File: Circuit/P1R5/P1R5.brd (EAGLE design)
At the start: 61 x 61 mm, 126 parts, among them U1 MK20DX256VLH7, Y1 32.768KHz, Y2 16Mhz/8pF

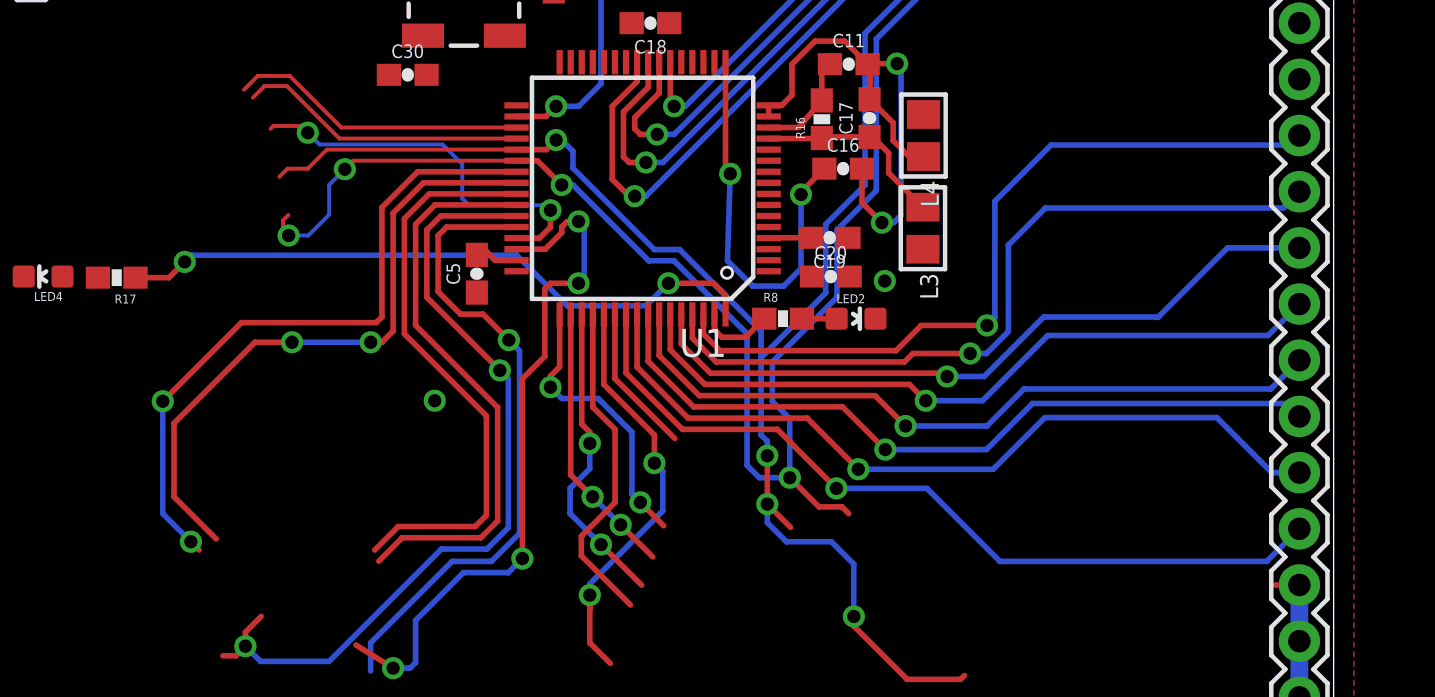
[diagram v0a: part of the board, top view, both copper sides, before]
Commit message: more cleanup on micro.
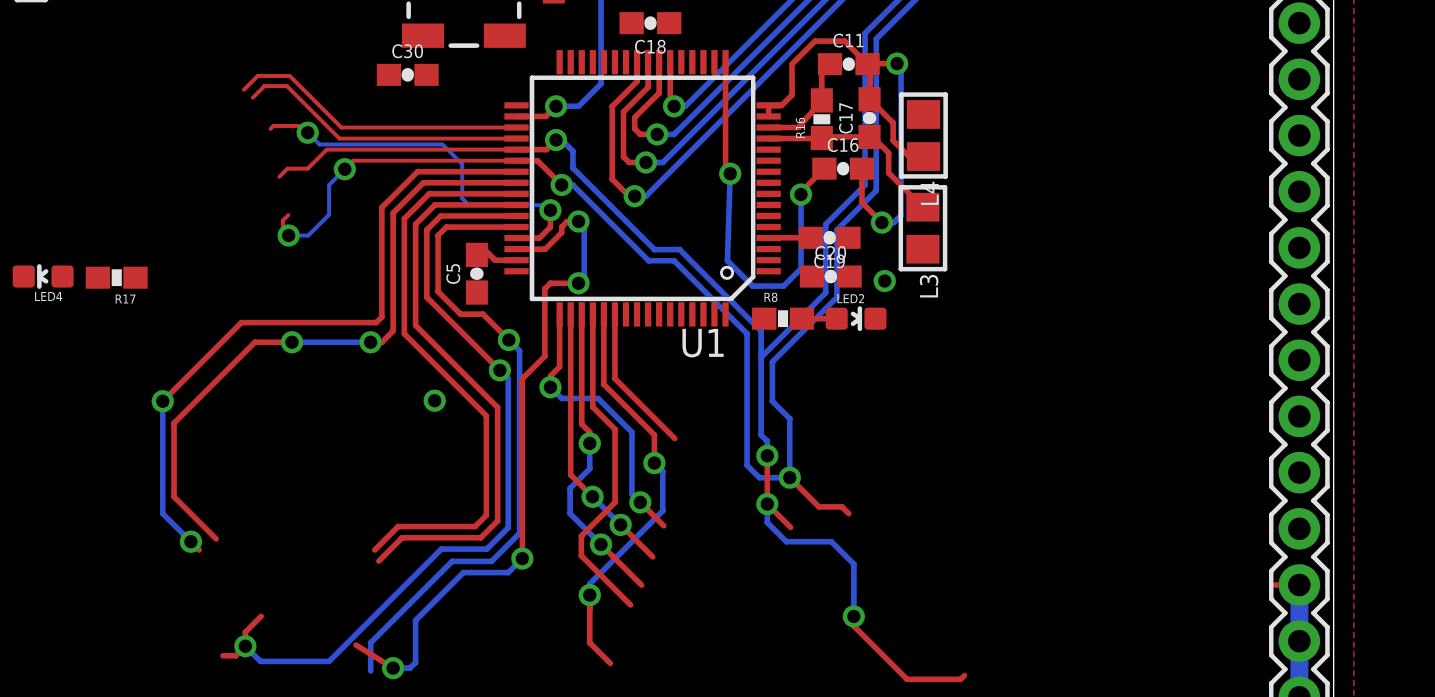
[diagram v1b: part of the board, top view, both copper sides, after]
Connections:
- net PTC10 renamed N$24
- net PTC11 renamed N$16
- net PTD0 renamed N$17
- net PTD1 renamed N$18
- net PTD2 renamed N$19
- net PTD3 renamed N$20
- net PTD4 renamed N$21
- net PTD5 renamed N$23
- removed net PTD6: R8.1, U1.63
- removed net PTD7: R17.1, U1.64
- new net N$10: LED2.C, U1.63
- new net N$13: LED4.C, U1.64
- net 3.3V: now also R17.1, R8.1
- net GND: no longer LED2.C, LED4.C
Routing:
- net N$24: track 37.2 -> 0.00 mm, vias 1 -> 0
- net N$16: track 36.2 -> 0.00 mm, vias 1 -> 0
- net N$23: track 35.3 -> 0.00 mm, vias 1 -> 0
- net N$21: track 34.4 -> 0.00 mm, vias 1 -> 0
- net N$17: track 34.3 -> 0.00 mm, vias 1 -> 0
- net N$18: track 33.4 -> 0.00 mm, vias 1 -> 0
- net N$19: track 32.8 -> 0.00 mm, vias 1 -> 0
- net N$20: track 32.3 -> 0.00 mm, vias 1 -> 0
- net PTD7: track 29.5 -> 0.00 mm, vias 2 -> 0
- net PTD6: track 3.43 -> 0.00 mm

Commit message: hierarchical blocks done.
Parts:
- removed IMU1:R13, IMU1:R14: 10k, SparkFun-Resistors:0603-RES
- added R13, R14: 10k, SparkFun-Resistors:0603-RES
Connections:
- net PTB0 renamed N$27
- net PTB1 renamed N$28
- net PTB16 renamed N$34
- net PTB17 renamed N$35
- net PTB18 renamed N$38
- net PTB19 renamed N$39
- net PTC1 renamed N$41
- net PTC3 renamed N$40
- net PTC4 renamed N$46
- net PTC5 renamed N$47
- net PTC6 renamed N$48
- net PTC7 renamed N$49
- net PTC8 renamed N$42
- net PTC9 renamed N$45
- removed net A12: U1.11
- removed net A13: U1.12
- removed net AD0: U1.45
- removed net DAC/A14: U1.18
- removed net IMU1:GND: IMU1:C24.1, IMU1:C25.2, IMU1:C27.1, IMU1:U3.18, IMU1:U3.20
- removed net LED_DRIVER1:GND: LED_DRIVER1:R19.2, LED_DRIVER1:R20.2, LED_DRIVER1:R21.2, LED_DRIVER1:R23.2, LED_DRIVER1:R24.2, LED_DRIVER1:U$20.9, LED_DRIVER1:U$21.9
- removed net MESH1:GND: MESH1:C10.2, MESH1:C12.2, MESH1:C14.2, MESH1:C15.2, MESH1:C36.2, MESH1:C37.1, MESH1:C8.1, MESH1:C9.2, MESH1:R12.2, MESH1:U$4.14, MESH1:U$4.17, MESH1:U$4.20, MESH1:U$4.8
- removed net PTA12: U1.28
- removed net PTA13: U1.29
- removed net PTA4: U1.26
- removed net PTA5: U1.27
- removed net PTC0: U1.43
- removed net PTE0: U1.1
- removed net PTE1: U1.2
- removed net SCL: U1.37
- removed net SDA: U1.38
- removed net USB_D_N: U1.6
- removed net USB_D_P: U1.5
- removed net WIFI1:GND: WIFI1:C22.1, WIFI1:C23.2, WIFI1:C26.1, WIFI1:C28.1, WIFI1:C33.2, WIFI1:C34.2, WIFI1:C35.2, WIFI1:C7.2, WIFI1:L7.2, WIFI1:L8.2, WIFI1:R1.2, WIFI1:R5.1, WIFI1:R51.1, WIFI1:U$3.4, WIFI1:U$6.GND
- new net N$25: R14.2, U1.37
- new net N$26: R13.2, U1.38
- net 3.3V: now also R13.1, R14.1
- net GND: now also IMU1:C24.1, IMU1:C25.2, IMU1:C27.1, IMU1:U3.18, IMU1:U3.20, LED_DRIVER1:R19.2, LED_DRIVER1:R20.2, LED_DRIVER1:R21.2, LED_DRIVER1:R23.2, LED_DRIVER1:R24.2, LED_DRIVER1:U$20.9, LED_DRIVER1:U$21.9, MESH1:C10.2, MESH1:C12.2, MESH1:C14.2, MESH1:C15.2, MESH1:C36.2, MESH1:C37.1, MESH1:C8.1, MESH1:C9.2, MESH1:R12.2, MESH1:U$4.14, MESH1:U$4.17, MESH1:U$4.20, MESH1:U$4.8, WIFI1:C22.1, WIFI1:C23.2, WIFI1:C26.1, WIFI1:C28.1, WIFI1:C33.2, WIFI1:C34.2, WIFI1:C35.2, WIFI1:C7.2, WIFI1:L7.2, WIFI1:L8.2, WIFI1:R1.2, WIFI1:R5.1, WIFI1:R51.1, WIFI1:U$3.4, WIFI1:U$6.GND
- net IMU1:N$1: no longer IMU1:R13.2
- net IMU1:N$2: no longer IMU1:R14.2
- net IMU1:N$6: no longer IMU1:R13.1, IMU1:R14.1
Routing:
- net SCL: track 87.3 -> 0.00 mm, vias 5 -> 0
- net SDA: track 78.5 -> 0.00 mm, vias 5 -> 0
- net PTC0: track 36.8 -> 0.00 mm, vias 2 -> 0
- net N$40: track 31.7 -> 0.00 mm, vias 4 -> 0
- net N$34: track 30.6 -> 0.00 mm, vias 2 -> 0
- net N$41: track 29.3 -> 0.00 mm, vias 1 -> 0
- net N$35: track 29.1 -> 0.00 mm, vias 2 -> 0
- net N$38: track 26.2 -> 0.00 mm
- net N$39: track 26.0 -> 0.00 mm
- net N$42: track 19.3 -> 0.00 mm, vias 2 -> 0
- net AD0: track 18.1 -> 0.00 mm, vias 2 -> 0
- net N$49: track 15.1 -> 0.00 mm
- net N$48: track 14.1 -> 0.00 mm, vias 2 -> 0
- net N$27: track 13.5 -> 0.00 mm
- net N$28: track 13.1 -> 0.00 mm
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
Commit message: labels made on all hierarchical blocks and nets
pretty much all connected back up. Not sure it's showing through on the
schematic yet.
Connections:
- new net N$50: U1.43
- new net WIFI1:N$25: WIFI1:C33.2, WIFI1:U$6.VDDA/1
- new net WIFI1:N$26: WIFI1:C26.2, WIFI1:U$6.VDD3P3/3
- new net WIFI1:N$27: WIFI1:C28.2, WIFI1:U$6.VDD3P3/4
- net 3.3V: now also WIFI1:R15.2
- net GND: now also WIFI1:C33.1; no longer WIFI1:C33.2
- net WIFI1:N$17: no longer WIFI1:C26.2, WIFI1:C28.2, WIFI1:C33.1, WIFI1:R15.2, WIFI1:U$6.VDD3P3/3, WIFI1:U$6.VDD3P3/4, WIFI1:U$6.VDDA/1
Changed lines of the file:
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@@
 <contactref element="WIFI1:C34" pad="2"/>
 <contactref element="WIFI1:L7" pad="2"/>
-<contactref element="WIFI1:C33" pad="2"/>
 <contactref element="WIFI1:C7" pad="2"/>
-<contactref element="WIFI1:C28" pad="1"/>
-<contactref element="WIFI1:C26" pad="1"/>
 <contactref element="WIFI1:C23" pad="2"/>
 <contactref element="WIFI1:R1" pad="2"/>
@@
 <contactref element="LED_DRIVER1:U$20" pad="9"/>
 <contactref element="LED_DRIVER1:U$21" pad="9"/>
+<contactref element="WIFI1:C33" pad="1"/>
+<contactref element="WIFI1:C26" pad="1"/>
+<contactref element="WIFI1:C28" pad="1"/>
 <wire x1="-22.8482" y1="-200.6854" x2="-22.8482" y2="-203.6572" width="0" layer="19" extent="1-1"/>
 <wire x1="-22.8482" y1="-194.7418" x2="-22.8482" y2="-200.6854" width="0" layer="19" extent="1-1"/>
@@
 <wire x1="-5.8302" y1="-55.88" x2="-7.5302" y2="-61.8236" width="0" layer="19" extent="1-1"/>
 <wire x1="-5.8302" y1="-52.9082" x2="-5.8302" y2="-55.88" width="0" layer="19" extent="1-1"/>
-<wire x1="-5.8302" y1="-49.9364" x2="-5.8302" y2="-52.9082" width="0" layer="19" extent="1-1"/>
-<wire x1="-7.5302" y1="-46.9646" x2="-5.8302" y2="-49.9364" width="0" layer="19" extent="1-1"/>
+<wire x1="-7.5302" y1="-49.9364" x2="-5.8302" y2="-52.9082" width="0" layer="19" extent="1-1"/>
+<wire x1="-7.5302" y1="-46.9646" x2="-7.5302" y2="-49.9364" width="0" layer="19" extent="1-1"/>
 <wire x1="-7.5302" y1="-43.9928" x2="-7.5302" y2="-46.9646" width="0" layer="19" extent="1-1"/>
 <wire x1="-5.588" y1="-40.0812" x2="-7.5302" y2="-43.9928" width="0" layer="19" extent="1-1"/>
@@
 <contactref element="R14" pad="1"/>
 <contactref element="R13" pad="1"/>
+<contactref element="WIFI1:R15" pad="2"/>
 <wire x1="45.466" y1="55.2958" x2="48.6814" y2="54.0258" width="0" layer="19" extent="1-1"/>
 <wire x1="36.307" y1="54.356" x2="45.466" y2="55.2958" width="0" layer="19" extent="1-1"/>
@@
 <wire x1="6.7936" y1="31.496" x2="24.018" y2="31.7846" width="0" layer="19" extent="1-1"/>
 <wire x1="58.3268" y1="17.6022" x2="42.3926" y2="32.7812" width="0" layer="19" extent="1-1"/>
-<wire x1="-7.5302" y1="-64.7954" x2="6.7936" y2="31.496" width="0" layer="19" extent="1-1"/>
+<wire x1="-5.8302" y1="-58.8518" x2="6.7936" y2="31.496" width="0" layer="19" extent="1-1"/>
+<wire x1="-7.5302" y1="-64.7954" x2="-5.8302" y2="-58.8518" width="0" layer="19" extent="1-1"/>
 <wire x1="-7.1492" y1="-68.0212" x2="-7.5302" y2="-64.7954" width="0" layer="19" extent="1-1"/>
 <wire x1="-11.0664" y1="-69.4454" x2="-7.1492" y2="-68.0212" width="0" layer="19" extent="1-1"/>
@@
 <contactref element="WIFI1:C22" pad="2"/>
 <contactref element="WIFI1:C34" pad="1"/>
-<contactref element="WIFI1:C33" pad="1"/>
-<contactref element="WIFI1:C28" pad="2"/>
-<contactref element="WIFI1:C26" pad="2"/>
 <contactref element="WIFI1:U$3" pad="8"/>
-<contactref element="WIFI1:R15" pad="2"/>
 <contactref element="WIFI1:C35" pad="1"/>
-<contactref element="WIFI1:U$6" pad="VDDA/1"/>
-<contactref element="WIFI1:U$6" pad="VDD3P3/3"/>
-<contactref element="WIFI1:U$6" pad="VDD3P3/4"/>
 <contactref element="WIFI1:U$6" pad="VDDPST/11"/>
 <contactref element="WIFI1:U$6" pad="VDDPST/17"/>
 <contactref element="WIFI1:U$6" pad="VDDD/29"/>
 <contactref element="WIFI1:U$6" pad="VDDA/30"/>
-<wire x1="-7.5302" y1="-55.88" x2="-5.8302" y2="-58.8518" width="0" layer="19" extent="1-1"/>
 <wire x1="-7.5302" y1="-52.9082" x2="-7.5302" y2="-55.88" width="0" layer="19" extent="1-1"/>
-<wire x1="-7.5302" y1="-49.9364" x2="-7.5302" y2="-52.9082" width="0" layer="19" extent="1-1"/>
-<wire x1="-5.8302" y1="-46.9646" x2="-7.5302" y2="-49.9364" width="0" layer="19" extent="1-1"/>
-<wire x1="-5.8302" y1="-43.9928" x2="-5.8302" y2="-46.9646" width="0" layer="19" extent="1-1"/>
-<wire x1="-6.338" y1="-42.3812" x2="-5.8302" y2="-43.9928" width="0" layer="19" extent="1-1"/>
-<wire x1="-7.888" y1="-39.8312" x2="-6.338" y2="-42.3812" width="0" layer="19" extent="1-1"/>
-<wire x1="-7.888" y1="-39.3312" x2="-7.888" y2="-39.8312" width="0" layer="19" extent="1-1"/>
-<wire x1="-7.888" y1="-38.3312" x2="-7.888" y2="-39.3312" width="0" layer="19" extent="1-1"/>
-<wire x1="-6.338" y1="-37.7812" x2="-7.888" y2="-38.3312" width="0" layer="19" extent="1-1"/>
+<wire x1="-6.338" y1="-42.3812" x2="-7.5302" y2="-52.9082" width="0" layer="19" extent="1-1"/>
+<wire x1="-3.288" y1="-41.8312" x2="-6.338" y2="-42.3812" width="0" layer="19" extent="1-1"/>
+<wire x1="-6.338" y1="-37.7812" x2="-6.338" y2="-42.3812" width="0" layer="19" extent="1-1"/>
 <wire x1="-5.838" y1="-37.7812" x2="-6.338" y2="-37.7812" width="0" layer="19" extent="1-1"/>
-<wire x1="-3.288" y1="-41.8312" x2="-6.338" y2="-42.3812" width="0" layer="19" extent="1-1"/>
 <wire x1="-5.8302" y1="-28.1686" x2="-5.838" y2="-37.7812" width="0" layer="19" extent="1-1"/>
 <wire x1="-3.388" y1="-22.9396" x2="-5.8302" y2="-28.1686" width="0" layer="19" extent="1-1"/>
@@
 </signal>
 <signal name="WIFI1:N$11">
-<contactref element="WIFI1:C7" pad="1"/>
 <contactref element="WIFI1:Y3" pad="1"/>
 <contactref element="WIFI1:U$6" pad="XTAL_OUT/27"/>
+<contactref element="WIFI1:C7" pad="1"/>
 <wire x1="-7.0062" y1="-20.7334" x2="-4.838" y2="-37.7812" width="0" layer="19" extent="1-1"/>
 <wire x1="-7.5302" y1="-15.4686" x2="-7.0062" y2="-20.7334" width="0" layer="19" extent="1-1"/>
@@
 <signal name="WIFI1:N$12">
 <contactref element="WIFI1:Y3" pad="3"/>
+<contactref element="WIFI1:U$6" pad="XTAL_IN/28"/>
 <contactref element="WIFI1:C23" pad="1"/>
-<contactref element="WIFI1:U$6" pad="XTAL_IN/28"/>
 <wire x1="-3.3062" y1="-18.4334" x2="-5.338" y2="-37.7812" width="0" layer="19" extent="1-1"/>
 <wire x1="-7.5302" y1="-12.4968" x2="-3.3062" y2="-18.4334" width="0" layer="19" extent="1-1"/>
@@
 <contactref element="U1" pad="52"/>
 </signal>
+<signal name="N$50">
+<contactref element="U1" pad="43"/>
+</signal>
+<signal name="WIFI1:N$25">
+<contactref element="WIFI1:C33" pad="2"/>
+<contactref element="WIFI1:U$6" pad="VDDA/1"/>
+<wire x1="-7.888" y1="-38.3312" x2="-5.8302" y2="-49.9364" width="0" layer="19" extent="1-1"/>
+</signal>
+<signal name="WIFI1:N$26">
+<contactref element="WIFI1:C26" pad="2"/>
+<contactref element="WIFI1:U$6" pad="VDD3P3/3"/>
+<wire x1="-7.888" y1="-39.3312" x2="-5.8302" y2="-43.9928" width="0" layer="19" extent="1-1"/>
+</signal>
+<signal name="WIFI1:N$27">
+<contactref element="WIFI1:C28" pad="2"/>
+<contactref element="WIFI1:U$6" pad="VDD3P3/4"/>
+<wire x1="-7.888" y1="-39.8312" x2="-5.8302" y2="-46.9646" width="0" layer="19" extent="1-1"/>
+</signal>
 </signals>

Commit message: moved libraries, regenerated PCB, reannotated design, connected hierarchical blocks.
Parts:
- removed C16, C18, C19, C21, VREG1:C2, VREG1:C4: 0.1uF, appfruits:0603-CAP
- removed C17, C20: 2.2uF, appfruits:0603-CAP
- removed C29, C30, C31, C32, VREG1:C1: 10uF, appfruits:0603-CAP
- removed IMU1:C24, IMU1:C25, IMU1:C27, MESH1:C36, MESH1:C37, WIFI1:C26, WIFI1:C28, WIFI1:C33, WIFI1:C34, WIFI1:C35: .1 uF, SparkFun-Capacitors:0603-CAP
- removed IMU1:U3: MPU-9250, chips:QFN-24/3MM
- removed JP5: (no value), SparkFun-Connectors:1X02
- removed L3, L4: 600 Ohm/100 Mhz, appfruits:0805
- removed LED4, VREG1:LED1: (no value), appfruits:LED-0603
- removed LED_DRIVER1:JP3: (no value), SparkFun:1X04
- removed LED_DRIVER1:R19, LED_DRIVER1:R20, LED_DRIVER1:R21, LED_DRIVER1:R22, LED_DRIVER1:R23, LED_DRIVER1:R24: 10k, SparkFun:0603-RES
- removed LED_DRIVER1:R25, LED_DRIVER1:R26, LED_DRIVER1:R27, LED_DRIVER1:R28, LED_DRIVER1:R29, LED_DRIVER1:R30, LED_DRIVER1:R31, LED_DRIVER1:R32, LED_DRIVER1:R33, LED_DRIVER1:R34, LED_DRIVER1:R35, LED_DRIVER1:R36, LED_DRIVER1:R37, LED_DRIVER1:R38, LED_DRIVER1:R39, LED_DRIVER1:R40, LED_DRIVER1:R41, LED_DRIVER1:R42, LED_DRIVER1:R43, LED_DRIVER1:R44, LED_DRIVER1:R45, LED_DRIVER1:R46, LED_DRIVER1:R47, LED_DRIVER1:R48, R49, R50, R52, R53: (no value), SparkFun:0402-RES
- removed LED_DRIVER1:U$11, LED_DRIVER1:U$13, LED_DRIVER1:U$14, LED_DRIVER1:U$15, LED_DRIVER1:U$16, LED_DRIVER1:U$17, LED_DRIVER1:U$18, LED_DRIVER1:U$8: LTST-C19FD1WT, led:LTST-C19FD1WT
- removed LED_DRIVER1:U$20, LED_DRIVER1:U$21: PCA9552BS, NXP_By_element14_Batch_1:HVQFN24
- removed MESH1:C10: 4.7 pF, SparkFun-Capacitors:0603-CAP
- removed MESH1:C12: 1.0 pF, SparkFun-Capacitors:0603-CAP
- removed MESH1:C13: 1.5 pF, SparkFun-Capacitors:0603-CAP
- removed MESH1:C14, MESH1:C15: 22 pF, SparkFun-Capacitors:0603-CAP
- removed MESH1:C8: 33 nF, SparkFun-Capacitors:0603-CAP
- removed MESH1:C9: 2.2 nF, SparkFun-Capacitors:0603-CAP
- removed MESH1:L2: 2.7 nH, SparkFun-Passives:C0402
- removed MESH1:L5: 8.2 nH, SparkFun-Passives:C0402
- removed MESH1:L6: 3.9 nH, SparkFun-Passives:C0402
- removed MESH1:R11: 1M, SparkFun-Resistors:0603-RES
- removed MESH1:R12: 22k, SparkFun-Resistors:0603-RES
- removed MESH1:U$2, WIFI1:U$1: ANTENNA2SMD, SparkFun-RF:ANTENNA-CHIP2
- removed MESH1:U$4: NRF24L01, RF:QFN20(4X4)
- removed MESH1:Y4: 16 Mhz, SparkFun-FreqCtrl:CRYSTAL-SMD-5X3
- removed R13, R14, WIFI1:R51: 10k, SparkFun-Resistors:0603-RES
- removed R16, R17, VREG1:R9: 470, appfruits:0603-RES
- removed U$7: 2X5_0.05"_CORTEX_DEBUGTH_NOKEY_UNSHROUDED, con-cortex:2X5_0.05"_TH_NS
- removed VREG1:C3: 22uF, appfruits:0603-CAP
- removed VREG1:L1: 2.2uH, 2.1A, appfruits:LPS3015
- removed VREG1:R3: 2M, appfruits:0603-RES
- removed VREG1:R4, VREG1:R6: 220K, appfruits:0603-RES
- removed VREG1:R7: 1.2M, appfruits:0603-RES
- removed VREG1:U2: TPS61200, appfruits:QFN-10_PAD
- removed WIFI1:C22: 1 uF, SparkFun-Capacitors:0603-CAP
- removed WIFI1:C23, WIFI1:C7: 15 pF, SparkFun-Capacitors:0603-CAP
- removed WIFI1:C6: 5.6 pF, SparkFun-Capacitors:0603-CAP
- removed WIFI1:L7, WIFI1:L8: (no value), SparkFun-Passives:0603
- removed WIFI1:R1, WIFI1:R15, WIFI1:R5: 12k, SparkFun-Resistors:0603-RES
- removed WIFI1:R18: 200, SparkFun-Resistors:0603-RES
- removed WIFI1:U$3: 25Q40, wifi:SOP8
- removed WIFI1:U$6: ESP8266EX, wifi:QFN32
- removed WIFI1:Y3: 26 Mhz, SparkFun-FreqCtrl:CRYSTAL-SMD-5X3
- added C1, C7: 2.2uF, appfruits:0603-CAP
- added C10, C101, C12, C9: 10uF, appfruits:0603-CAP
- added C102, C104, C2, C3, C4, C6, C8: 0.1uF, appfruits:0603-CAP
- added C103: 22uF, appfruits:0603-CAP
- added C206: 5.6 pF, SparkFun-Capacitors:0603-CAP
- added C207, C223: 15 pF, SparkFun-Capacitors:0603-CAP
- added C222: 1 uF, SparkFun-Capacitors:0603-CAP
- added C226, C228, C233, C234, C235, C336, C337, C424, C425, C427: .1 uF, SparkFun-Capacitors:0603-CAP
- added C308: 33 nF, SparkFun-Capacitors:0603-CAP
- added C309: 2.2 nF, SparkFun-Capacitors:0603-CAP
- added C310: 4.7 pF, SparkFun-Capacitors:0603-CAP
- added C312: 1.0 pF, SparkFun-Capacitors:0603-CAP
- added C313: 1.5 pF, SparkFun-Capacitors:0603-CAP
- added C314, C315: 22 pF, SparkFun-Capacitors:0603-CAP
- added J1: 2X5_0.05"_CORTEX_DEBUGTH_NOKEY_UNSHROUDED, con-cortex:2X5_0.05"_TH_NS
- added JP2: (no value), SparkFun-Connectors:1X15
- added JP503: (no value), SparkFun:1X04
- added L1, L2: 600 Ohm/100 Mhz, appfruits:0805
- added L101: 2.2uH, 2.1A, appfruits:LPS3015
- added L207, L208: DNP, SparkFun-Passives:0603
- added L302: 2.7 nH, SparkFun-Passives:C0402
- added L305: 8.2 nH, SparkFun-Passives:C0402
- added L306: 3.9 nH, SparkFun-Passives:C0402
- added LED1, LED101: (no value), appfruits:LED-0603
- added R1, R109, R6, R7: 470, appfruits:0603-RES
- added R103: 2M, appfruits:0603-RES
- added R104, R106: 220K, appfruits:0603-RES
- added R107: 1.2M, appfruits:0603-RES
- added R2, R3, R4, R5, R525, R526, R527, R528, R529, R530, R531, R532, R533, R534, R535, R536, R537, R538, R539, R540, R541, R542, R543, R544, R545, R546, R547, R548: (no value), SparkFun:0402-RES
- added R201, R205, R215: 12k, SparkFun-Resistors:0603-RES
- added R218: 200, SparkFun-Resistors:0603-RES
- added R251, R9: 10k, SparkFun-Resistors:0603-RES
- added R311: 1M, SparkFun-Resistors:0603-RES
- added R312: 22k, SparkFun-Resistors:0603-RES
- added R519, R520, R521, R522, R523, R524: 10k, SparkFun:0603-RES
- added U$201, U$302: ANTENNA2SMD, SparkFun-RF:ANTENNA-CHIP2
- added U$203: 25Q40, wifi:SOP8
- added U$206: ESP8266EX, wifi:QFN32
- added U$304: NRF24L01, RF:QFN20(4X4)
- added U$508, U$511, U$513, U$514, U$515, U$516, U$517, U$518: LTST-C19FD1WT, led:LTST-C19FD1WT
- added U$520, U$521: PCA9552BS, NXP_By_element14_Batch_1:HVQFN24
- added U102: TPS61200, appfruits:QFN-10_PAD
- added U403: MPU-9250, chips:QFN-24/3MM
- added Y203: 26 Mhz, SparkFun-FreqCtrl:CRYSTAL-SMD-5X3
- added Y304: 16 Mhz, SparkFun-FreqCtrl:CRYSTAL-SMD-5X3
- C11: value 0.1uF -> 10uF
- JP1: device SparkFun-Connectors:1X15 -> SparkFun-Connectors:1X02
- R8: value 470 -> 10k; device appfruits:0603-RES -> SparkFun-Resistors:0603-RES
- Y1: value 32.768KHz -> 16Mhz/8pF; device appfruits:CRYSTAL-TXC-7A -> appfruits:CRYSTAL-SMD-5X3
- Y2: value 16Mhz/8pF -> 32.768KHz; device appfruits:CRYSTAL-SMD-5X3 -> appfruits:CRYSTAL-TXC-7A
- moved JP1 118.8 mm to (-57.1, 71.1), turned to 0 degrees
- moved C11 95.7 mm to (-49.5, 77.5)
- moved R8 91.4 mm to (-39.4, 81.3)
- moved LED2 81.8 mm to (-24.1, 81.3), turned to 0 degrees
- moved S1 70.7 mm to (-68.6, 66.0), turned to 0 degrees
- moved C5 67.0 mm to (-26.7, 77.5), turned to 0 degrees
- moved Y1 66.1 mm to (-31.8, 66.0), turned to 0 degrees
- moved U1 61.2 mm to (-25.4, 8.89), turned to 0 degrees
- moved Y2 53.6 mm to (-16.5, 81.3)
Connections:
- removed net IMU1:N$1: IMU1:U3.24
- removed net IMU1:N$2: IMU1:U3.23
- removed net IMU1:N$3: IMU1:U3.11
- removed net IMU1:N$5: IMU1:U3.12
- removed net IMU1:N$6: IMU1:C24.2, IMU1:C25.1, IMU1:U3.1, IMU1:U3.13, IMU1:U3.22, IMU1:U3.8
- removed net IMU1:N$7: IMU1:U3.9
- removed net LED_DRIVER1:N$31: LED_DRIVER1:U$20.20, LED_DRIVER1:U$21.20
- removed net LED_DRIVER1:N$32: LED_DRIVER1:U$20.19, LED_DRIVER1:U$21.19
- removed net LED_DRIVER1:N$34: LED_DRIVER1:U$20.21, LED_DRIVER1:U$21.21
- removed net LED_DRIVER1:N$35: LED_DRIVER1:U$21.16
- removed net LED_DRIVER1:N$36: LED_DRIVER1:U$21.17
- removed net LED_DRIVER1:V+: LED_DRIVER1:R22.2, LED_DRIVER1:U$11.V, LED_DRIVER1:U$13.V, LED_DRIVER1:U$14.V, LED_DRIVER1:U$15.V, LED_DRIVER1:U$16.V, LED_DRIVER1:U$17.V, LED_DRIVER1:U$18.V, LED_DRIVER1:U$8.V
- removed net MESH1:N$15: MESH1:C36.1, MESH1:C37.2, MESH1:U$4.15, MESH1:U$4.18, MESH1:U$4.7
- removed net MESH1:N$2: MESH1:U$4.2
- removed net MESH1:N$3: MESH1:U$4.3
- removed net MESH1:N$4: MESH1:U$4.4
- removed net MESH1:N$5: MESH1:U$4.5
- removed net MESH1:N$6: MESH1:U$4.6
- removed net MESH1:N$9: MESH1:L2.2
- removed net N$11: C18.1, C21.1, C5.1
- removed net N$19: JP1.8, U1.59
- removed net N$25: R14.2, U1.37
- removed net N$26: R13.2, U1.38
- removed net N$27: U1.35
- removed net N$28: U1.36
- removed net N$32: S1.2, VREG1:C1.1, VREG1:C2.1, VREG1:L1.2, VREG1:R3.2, VREG1:U2.5, VREG1:U2.6, VREG1:U2.8
- removed net N$34: U1.39
- removed net N$35: U1.40
- removed net N$38: U1.41
- removed net N$39: U1.42
- removed net N$40: U1.46
- removed net N$41: U1.44
- removed net N$42: U1.53
- removed net N$45: U1.54
- removed net N$46: U1.49
- removed net N$47: U1.50
- removed net N$48: U1.51
- removed net N$49: U1.52
- removed net N$50: U1.43
- removed net WIFI1:N$1: WIFI1:U$3.1, WIFI1:U$6.SD_CMD/20
- removed net WIFI1:N$10: WIFI1:U$6.U0TXD/26
- removed net WIFI1:N$13: WIFI1:R1.1, WIFI1:U$6.RES12K/31
- removed net WIFI1:N$15: WIFI1:U$6.GPIO2/14
- removed net WIFI1:N$17: WIFI1:C22.2, WIFI1:C34.1, WIFI1:C35.1, WIFI1:U$3.8, WIFI1:U$6.VDDA/30, WIFI1:U$6.VDDD/29, WIFI1:U$6.VDDPST/11, WIFI1:U$6.VDDPST/17
- removed net WIFI1:N$18: WIFI1:U$6.CHIP_EN/7
- removed net WIFI1:N$19: WIFI1:R15.1, WIFI1:U$6.EXT_RSTB/32
- removed net WIFI1:N$2: WIFI1:U$3.2, WIFI1:U$6.SD_DATA_0/22
- removed net WIFI1:N$20: WIFI1:U$6.GPIO0/15
- removed net WIFI1:N$21: WIFI1:R18.1, WIFI1:U$3.6
- removed net WIFI1:N$23: WIFI1:U$6.U0RXD/25
- removed net WIFI1:N$24: WIFI1:U$6.XPD_DCDC/8
- removed net WIFI1:N$3: WIFI1:U$3.3, WIFI1:U$6.SD_DATA_3/19
- removed net WIFI1:N$4: WIFI1:U$3.7, WIFI1:U$6.SD_DATA_2/18
- removed net WIFI1:N$6: WIFI1:U$3.5, WIFI1:U$6.SD_DATA_1/23
- removed net WIFI1:N$9: WIFI1:U$6.TOUT/6
- new net CE: U$304.1, U1.54
- new net CHANGE: JP2.8, U1.59
- new net CHIP_EN: U$206.CHIP_EN/7, U1.44
- new net CSN: U$304.2, U1.49
- new net FSYNC: U1.36, U403.11
- new net GPIO0: U$206.GPIO0/15, U1.41
- new net GPIO2: U$206.GPIO2/14, U1.42
- new net INT: U1.35, U403.12
- new net IRQ: U$304.6, U1.53
- new net MISO: U$304.5, U1.52
- new net MOSI: U$304.4, U1.51
- new net N$3: U1.45, U403.22
- new net N$4: R8.2, U$520.19, U$521.19, U1.37, U403.23
- new net SCK: U$304.3, U1.50
- new net SDA: R9.2, U$520.20, U$521.20, U1.38, U403.24
- new net U0RX: U$206.U0RXD/25, U1.40
- new net U0TX: U$206.U0TXD/26, U1.39
- new net V_IN: C101.1, C102.1, L101.2, R103.2, S1.2, U102.5, U102.6, U102.8
- new net WIFI1:CLK: R218.1, U$203.6
- new net WIFI1:CS: U$203.1, U$206.SD_CMD/20
- new net WIFI1:D0: U$203.2, U$206.SD_DATA_0/22
- new net WIFI1:DIO: U$203.5, U$206.SD_DATA_1/23
- new net WIFI1:HOLD#: U$203.7, U$206.SD_DATA_2/18
- new net WIFI1:WP#: U$203.3, U$206.SD_DATA_3/19
- new net WIFI_RESET: R215.1, U$206.EXT_RSTB/32, U1.43
- new net XPD_DCDC: U$206.XPD_DCDC/8, U1.46
- net 3.3V: now also C103.1, C2.1, C222.2, C234.1, C235.1, C3.1, C336.1, C337.2, C4.1, C424.2, C425.1, C5.1, C7.1, J1.1, JP2.13, JP2.14, JP2.15, L1.2, R107.2, R109.1, R2.1, R215.2, R4.1, R5.1, R522.2, R6.1, R7.1, R9.1, U$203.8, U$206.VDDA/30, U$206.VDDD/29, U$206.VDDPST/11, U$206.VDDPST/17, U$304.15, U$304.18, U$304.7, U$508.V, U$511.V, U$513.V, U$514.V, U$515.V, U$516.V, U$517.V, U$518.V, U$520.21, U$521.21, U102.2, U403.1, U403.13, U403.8; no longer C19.1, C20.1, JP1.13, JP1.14, JP1.15, L3.2, R13.1, R14.1, R17.1, R49.1, R52.1, R53.1, U$7.1, VREG1:C3.1, VREG1:R7.2, VREG1:R9.1, VREG1:U2.2, WIFI1:R15.2
- net GND: now also C10.1, C101.2, C103.2, C104.2, C11.1, C12.1, C2.2, C207.2, C222.1, C223.2, C226.1, C228.1, C233.1, C234.2, C235.2, C3.2, C308.1, C309.2, C310.2, C312.2, C314.2, C315.2, C336.2, C337.1, C4.2, C424.1, C425.2, C427.1, C7.2, C9.1, J1.3, J1.5, J1.9, JP2.1, JP2.2, JP2.3, JP2.4, L2.1, L207.2, L208.2, LED101.C, R104.1, R106.1, R201.2, R205.1, R251.1, R3.1, R312.2, R519.2, R520.2, R521.2, R523.2, R524.2, U$203.4, U$206.GND, U$304.14, U$304.17, U$304.20, U$304.8, U$520.9, U$521.9, U102.11, U102.12, U102.13, U102.14, U102.15, U102.4, U102.9, U403.18, U403.20, U403.9; no longer C18.2, C19.2, C20.2, C21.2, C29.1, C30.1, C31.1, C32.1, IMU1:C24.1, IMU1:C25.2, IMU1:C27.1, IMU1:U3.18, IMU1:U3.20, JP1.1, JP1.3, JP1.4, L4.1, LED_DRIVER1:R19.2, LED_DRIVER1:R20.2, LED_DRIVER1:R21.2, LED_DRIVER1:R23.2, LED_DRIVER1:R24.2, LED_DRIVER1:U$20.9, LED_DRIVER1:U$21.9, MESH1:C10.2, MESH1:C12.2, MESH1:C14.2, MESH1:C15.2, MESH1:C36.2, MESH1:C37.1, MESH1:C8.1, MESH1:C9.2, MESH1:R12.2, MESH1:U$4.14, MESH1:U$4.17, MESH1:U$4.20, MESH1:U$4.8, R50.1, U$7.3, U$7.5, U$7.9, VREG1:C1.2, VREG1:C3.2, VREG1:C4.2, VREG1:LED1.C, VREG1:R4.1, VREG1:R6.1, VREG1:U2.11, VREG1:U2.12, VREG1:U2.13, VREG1:U2.14, VREG1:U2.15, VREG1:U2.4, VREG1:U2.9, WIFI1:C22.1, WIFI1:C23.2, WIFI1:C26.1, WIFI1:C28.1, WIFI1:C33.1, WIFI1:C34.2, WIFI1:C35.2, WIFI1:C7.2, WIFI1:L7.2, WIFI1:L8.2, WIFI1:R1.2, WIFI1:R5.1, WIFI1:R51.1, WIFI1:U$3.4, WIFI1:U$6.GND
- net IMU1:N$4: now also C427.2, U403.10; no longer IMU1:C27.2, IMU1:U3.10
- net LED_DRIVER1:N$1: now also R527.1, U$520.3; no longer LED_DRIVER1:R27.1, LED_DRIVER1:U$20.3
- net LED_DRIVER1:N$10: now also R535.1, U$520.11; no longer LED_DRIVER1:R35.1, LED_DRIVER1:U$20.11
- net LED_DRIVER1:N$11: now also R536.1, U$520.12; no longer LED_DRIVER1:R36.1, LED_DRIVER1:U$20.12
- net LED_DRIVER1:N$12: now also R534.1, U$520.13; no longer LED_DRIVER1:R34.1, LED_DRIVER1:U$20.13
- net LED_DRIVER1:N$13: now also JP503.4, U$520.14; no longer LED_DRIVER1:JP3.4, LED_DRIVER1:U$20.14
- net LED_DRIVER1:N$14: now also R520.1, U$520.23; no longer LED_DRIVER1:R20.1, LED_DRIVER1:U$20.23
- net LED_DRIVER1:N$15: now also R521.1, U$520.22; no longer LED_DRIVER1:R21.1, LED_DRIVER1:U$20.22
- net LED_DRIVER1:N$16: now also R538.1, U$521.1; no longer LED_DRIVER1:R38.1, LED_DRIVER1:U$21.1
- net LED_DRIVER1:N$17: now also R539.1, U$521.2; no longer LED_DRIVER1:R39.1, LED_DRIVER1:U$21.2
- net LED_DRIVER1:N$18: now also R537.1, U$521.3; no longer LED_DRIVER1:R37.1, LED_DRIVER1:U$21.3
- net LED_DRIVER1:N$19: now also R541.1, U$521.4; no longer LED_DRIVER1:R41.1, LED_DRIVER1:U$21.4
- net LED_DRIVER1:N$2: now also R526.1, U$520.1; no longer LED_DRIVER1:R26.1, LED_DRIVER1:U$20.1
- net LED_DRIVER1:N$20: now also R542.1, U$521.5; no longer LED_DRIVER1:R42.1, LED_DRIVER1:U$21.5
- net LED_DRIVER1:N$21: now also R540.1, U$521.6; no longer LED_DRIVER1:R40.1, LED_DRIVER1:U$21.6
- net LED_DRIVER1:N$22: now also R544.1, U$521.7; no longer LED_DRIVER1:R44.1, LED_DRIVER1:U$21.7
- net LED_DRIVER1:N$23: now also R545.1, U$521.8; no longer LED_DRIVER1:R45.1, LED_DRIVER1:U$21.8
- net LED_DRIVER1:N$24: now also R543.1, U$521.10; no longer LED_DRIVER1:R43.1, LED_DRIVER1:U$21.10
- net LED_DRIVER1:N$25: now also R547.1, U$521.11; no longer LED_DRIVER1:R47.1, LED_DRIVER1:U$21.11
- net LED_DRIVER1:N$26: now also R548.1, U$521.12; no longer LED_DRIVER1:R48.1, LED_DRIVER1:U$21.12
- net LED_DRIVER1:N$27: now also R546.1, U$521.13; no longer LED_DRIVER1:R46.1, LED_DRIVER1:U$21.13
- net LED_DRIVER1:N$28: now also R524.1, U$521.24; no longer LED_DRIVER1:R24.1, LED_DRIVER1:U$21.24
- net LED_DRIVER1:N$29: now also R523.1, U$521.23; no longer LED_DRIVER1:R23.1, LED_DRIVER1:U$21.23
- net LED_DRIVER1:N$3: now also R528.1, U$520.6; no longer LED_DRIVER1:R28.1, LED_DRIVER1:U$20.6
- net LED_DRIVER1:N$30: now also R522.1, U$521.22; no longer LED_DRIVER1:R22.1, LED_DRIVER1:U$21.22
- net LED_DRIVER1:N$33: now also R519.1, U$520.24; no longer LED_DRIVER1:R19.1, LED_DRIVER1:U$20.24
- net LED_DRIVER1:N$37: now also JP503.2, U$520.16; no longer LED_DRIVER1:JP3.2, LED_DRIVER1:U$20.16
- net LED_DRIVER1:N$38: now also JP503.1, U$520.17; no longer LED_DRIVER1:JP3.1, LED_DRIVER1:U$20.17
- net LED_DRIVER1:N$39: now also JP503.3, U$520.15; no longer LED_DRIVER1:JP3.3, LED_DRIVER1:U$20.15
- net LED_DRIVER1:N$4: now also R525.1, U$520.2; no longer LED_DRIVER1:R25.1, LED_DRIVER1:U$20.2
- net LED_DRIVER1:N$47: now also R529.2, U$511.R; no longer LED_DRIVER1:R29.2, LED_DRIVER1:U$11.R
- net LED_DRIVER1:N$48: now also R541.2, U$516.R; no longer LED_DRIVER1:R41.2, LED_DRIVER1:U$16.R
- net LED_DRIVER1:N$49: now also R547.2, U$518.R; no longer LED_DRIVER1:R47.2, LED_DRIVER1:U$18.R
- net LED_DRIVER1:N$5: now also R529.1, U$520.4; no longer LED_DRIVER1:R29.1, LED_DRIVER1:U$20.4
- net LED_DRIVER1:N$50: now also R543.2, U$517.B; no longer LED_DRIVER1:R43.2, LED_DRIVER1:U$17.B
- net LED_DRIVER1:N$51: now also R532.2, U$513.R; no longer LED_DRIVER1:R32.2, LED_DRIVER1:U$13.R
- net LED_DRIVER1:N$52: now also R535.2, U$514.R; no longer LED_DRIVER1:R35.2, LED_DRIVER1:U$14.R
- net LED_DRIVER1:N$53: now also R531.2, U$513.B; no longer LED_DRIVER1:R31.2, LED_DRIVER1:U$13.B
- net LED_DRIVER1:N$54: now also R533.2, U$513.G; no longer LED_DRIVER1:R33.2, LED_DRIVER1:U$13.G
- net LED_DRIVER1:N$55: now also R528.2, U$511.B; no longer LED_DRIVER1:R28.2, LED_DRIVER1:U$11.B
- net LED_DRIVER1:N$56: now also R530.2, U$511.G; no longer LED_DRIVER1:R30.2, LED_DRIVER1:U$11.G
- net LED_DRIVER1:N$57: now also R548.2, U$518.G; no longer LED_DRIVER1:R48.2, LED_DRIVER1:U$18.G
- net LED_DRIVER1:N$58: now also R537.2, U$515.B; no longer LED_DRIVER1:R37.2, LED_DRIVER1:U$15.B
- net LED_DRIVER1:N$59: now also R542.2, U$516.G; no longer LED_DRIVER1:R42.2, LED_DRIVER1:U$16.G
- net LED_DRIVER1:N$6: now also R530.1, U$520.5; no longer LED_DRIVER1:R30.1, LED_DRIVER1:U$20.5
- net LED_DRIVER1:N$60: now also R526.2, U$508.R; no longer LED_DRIVER1:R26.2, LED_DRIVER1:U$8.R
- net LED_DRIVER1:N$61: now also R536.2, U$514.G; no longer LED_DRIVER1:R36.2, LED_DRIVER1:U$14.G
- net LED_DRIVER1:N$62: now also R545.2, U$517.G; no longer LED_DRIVER1:R45.2, LED_DRIVER1:U$17.G
- net LED_DRIVER1:N$63: now also R534.2, U$514.B; no longer LED_DRIVER1:R34.2, LED_DRIVER1:U$14.B
- net LED_DRIVER1:N$64: now also R539.2, U$515.G; no longer LED_DRIVER1:R39.2, LED_DRIVER1:U$15.G
- net LED_DRIVER1:N$65: now also R527.2, U$508.B; no longer LED_DRIVER1:R27.2, LED_DRIVER1:U$8.B
- net LED_DRIVER1:N$66: now also R525.2, U$508.G; no longer LED_DRIVER1:R25.2, LED_DRIVER1:U$8.G
- net LED_DRIVER1:N$67: now also R544.2, U$517.R; no longer LED_DRIVER1:R44.2, LED_DRIVER1:U$17.R
- net LED_DRIVER1:N$68: now also R540.2, U$516.B; no longer LED_DRIVER1:R40.2, LED_DRIVER1:U$16.B
- net LED_DRIVER1:N$69: now also R538.2, U$515.R; no longer LED_DRIVER1:R38.2, LED_DRIVER1:U$15.R
- net LED_DRIVER1:N$7: now also R532.1, U$520.7; no longer LED_DRIVER1:R32.1, LED_DRIVER1:U$20.7
- net LED_DRIVER1:N$70: now also R546.2, U$518.B; no longer LED_DRIVER1:R46.2, LED_DRIVER1:U$18.B
- net LED_DRIVER1:N$8: now also R533.1, U$520.8; no longer LED_DRIVER1:R33.1, LED_DRIVER1:U$20.8
- net LED_DRIVER1:N$9: now also R531.1, U$520.10; no longer LED_DRIVER1:R31.1, LED_DRIVER1:U$20.10
- net MESH1:N$1: now also C309.1, C310.1, L302.2, U$304.11; no longer MESH1:U$4.1
- net MESH1:N$10: now also L305.1, L306.1, U$304.13; no longer MESH1:U$4.13
- net MESH1:N$11: now also R312.1, U$304.16; no longer MESH1:R12.1, MESH1:U$4.16
- net MESH1:N$12: now also C308.2, U$304.19; no longer MESH1:C8.2, MESH1:U$4.19
- net MESH1:N$13: now also L302.1, L305.2, U$304.12; no longer MESH1:L2.1, MESH1:L5.2, MESH1:U$4.12
- net MESH1:N$14: now also C312.1, C313.2, U$302.FEED; no longer MESH1:C12.1, MESH1:C13.2, MESH1:U$2.FEED
- net MESH1:N$24: now also C313.1, L306.2; no longer MESH1:C13.1, MESH1:L6.2
- net MESH1:N$7: now also C314.1, R311.1, U$304.9, Y304.1; no longer MESH1:C14.1, MESH1:R11.1, MESH1:U$4.9, MESH1:Y4.1
- net MESH1:N$8: now also C315.1, R311.2, U$304.10, Y304.3; no longer MESH1:C15.1, MESH1:R11.2, MESH1:U$4.10, MESH1:Y4.3
- net N$1: now also C11.2, Y2.P$2; no longer C31.2, Y1.P$2
- net N$10: now also LED1.C; no longer LED2.C
- net N$110: now also JP1.1; no longer JP5.1
- net N$13: now also LED2.C; no longer LED4.C
- net N$16: now also JP2.11; no longer JP1.11
- net N$17: now also JP2.10; no longer JP1.10
- net N$18: now also JP2.9; no longer JP1.9
- net N$2: now also C12.2, Y2.P$1; no longer C32.2, Y1.P$1
- net N$20: now also JP2.7; no longer JP1.7
- net N$21: now also JP2.6; no longer JP1.6
- net N$23: now also JP2.5; no longer JP1.5
- net N$24: now also JP2.12; no longer JP1.12
- net N$29: now also LED2.A, R7.2; no longer LED4.A, R17.2
- net N$7: now also LED1.A, R6.2; no longer LED2.A, R8.2
- net N$8: now also C9.2, Y1.3; no longer C29.2, Y2.3
- net N$9: now also C10.2, Y1.1; no longer C30.2, Y2.1
- net PTA0: now also J1.4, R3.2; no longer R50.2, U$7.4
- net PTA1: now also J1.8, R4.2; no longer R52.2, U$7.8
- net PTA2: now also J1.6; no longer U$7.6
- net PTA3: now also J1.2, R2.2; no longer R49.2, U$7.2
- net RESET_B: now also J1.10, R5.2; no longer R53.2, U$7.10
- net VDDA: now also C1.1, L1.1, R1.1; no longer C17.1, L3.1, R16.1
- net VREFH: now also C6.1, R1.2; no longer C11.1, R16.2
- net VREFL: now also C1.2, C6.2, C8.2, L2.2; no longer C11.2, C16.2, C17.2, L4.2
- net VREF_OUT: now also C8.1; no longer C16.1
- net VREG1:N$1: now also L101.1, U102.3; no longer VREG1:L1.1, VREG1:U2.3
- net VREG1:N$2: now also C104.1, U102.1; no longer VREG1:C4.1, VREG1:U2.1
- net VREG1:N$3: now also C102.2, R103.1, R104.2, U102.7; no longer VREG1:C2.2, VREG1:R3.1, VREG1:R4.2, VREG1:U2.7
- net VREG1:N$4: now also R106.2, R107.1, U102.10; no longer VREG1:R6.2, VREG1:R7.1, VREG1:U2.10
- net VREG1:N$5: now also LED101.A, R109.2; no longer VREG1:LED1.A, VREG1:R9.2
- net WIFI1:N$11: now also C207.1, U$206.XTAL_OUT/27, Y203.1; no longer WIFI1:C7.1, WIFI1:U$6.XTAL_OUT/27, WIFI1:Y3.1
- net WIFI1:N$12: now also C223.1, U$206.XTAL_IN/28, Y203.3; no longer WIFI1:C23.1, WIFI1:U$6.XTAL_IN/28, WIFI1:Y3.3
- net WIFI1:N$14: now also C206.1, L207.1, U$201.FEED; no longer WIFI1:C6.1, WIFI1:L7.1, WIFI1:U$1.FEED
- net WIFI1:N$16: now also R205.2, U$206.MTCK/12; no longer WIFI1:R5.2, WIFI1:U$6.MTCK/12
- net WIFI1:N$22: now also R251.2, U$206.MTDO/13; no longer WIFI1:R51.2, WIFI1:U$6.MTDO/13
- net WIFI1:N$25: now also C233.2, U$206.VDDA/1; no longer WIFI1:C33.2, WIFI1:U$6.VDDA/1
- net WIFI1:N$26: now also C226.2, U$206.VDD3P3/3; no longer WIFI1:C26.2, WIFI1:U$6.VDD3P3/3
- net WIFI1:N$27: now also C228.2, U$206.VDD3P3/4; no longer WIFI1:C28.2, WIFI1:U$6.VDD3P3/4
- net WIFI1:N$5: now also R218.2, U$206.SD_CLK/21; no longer WIFI1:R18.2, WIFI1:U$6.SD_CLK/21
- net WIFI1:N$7: now also C206.2, L208.1, U$206.LNA/2; no longer WIFI1:C6.2, WIFI1:L8.1, WIFI1:U$6.LNA/2
- net WIFI1:N$8: now also R201.1, U$206.RES12K/31; no longer WIFI1:U$6.VDD_RTC/5
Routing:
- net PTA3: track 34.8 -> 0.00 mm, vias 1 -> 0
- net RESET_B: track 32.1 -> 0.00 mm, vias 3 -> 0
- net PTA1: track 30.2 -> 0.00 mm, vias 1 -> 0
- net PTA2: track 29.0 -> 0.00 mm, vias 1 -> 0
- net PTA0: track 27.1 -> 0.00 mm, vias 2 -> 0
- net VREFL: track 25.1 -> 0.00 mm, vias 2 -> 0
- net VREF_OUT: track 18.2 -> 0.00 mm, vias 2 -> 0
- net VDDA: track 9.37 -> 0.00 mm
- net 3.3V: track 7.82 -> 0.00 mm
- net GND: track 4.98 -> 0.00 mm, vias 3 -> 0
- net VREFH: track 4.76 -> 0.00 mm
- net N$7: track 1.58 -> 0.00 mm
- removed copper zone on layer 15, net 3.3V
- removed copper zone on layer 1, net GND
- removed copper zone on layer 2, net GND
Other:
- board size 61 x 61 mm -> 160 x 100 mm
